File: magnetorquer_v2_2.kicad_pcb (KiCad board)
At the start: 2 copper layers, 89.9 x 96 mm, 25 parts, among them J1 Conn_01x07_Female, U1 MSP430FR5994IPN, U2 Payload, U3 LSM6DS3TR-C, U4 DRV_H3, U5 DRV_H2, U6 DRV_H1, Y1 Crystal

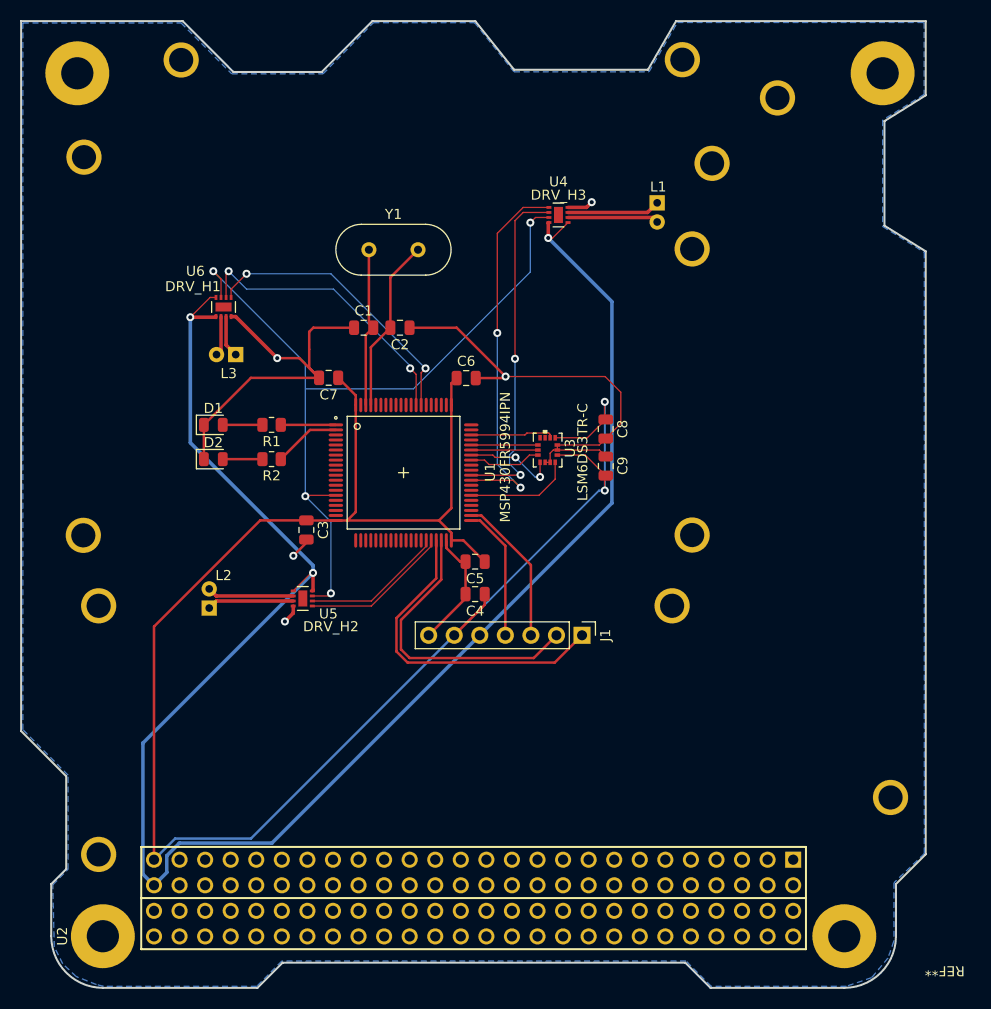
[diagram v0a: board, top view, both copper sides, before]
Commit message: added coils
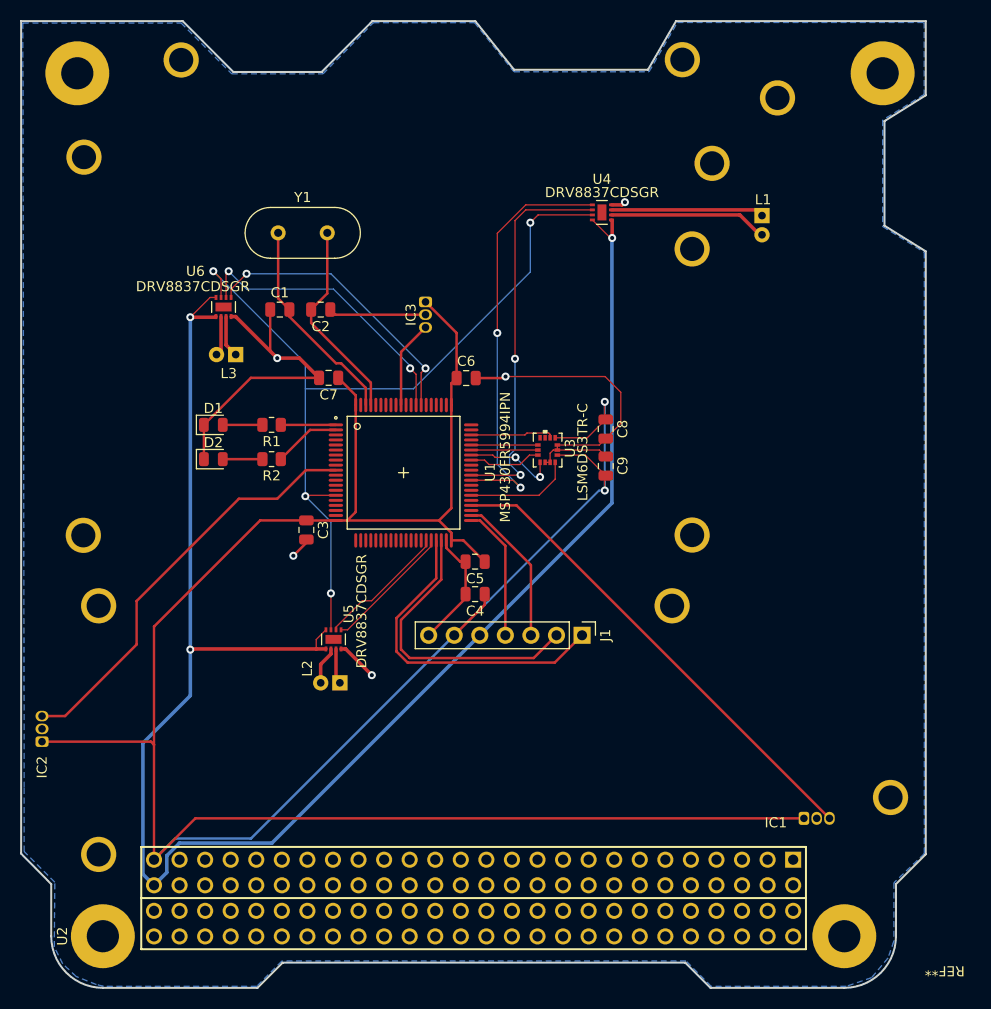
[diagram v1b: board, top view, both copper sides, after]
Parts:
- added IC1: AH9247Z3-G1, Package_TO_SOT_THT:TO-92Flat, B.Cu at (169.7, 135.9)
- added IC2: AH9247Z3-G1, Package_TO_SOT_THT:TO-92Flat, B.Cu at (94.0, 128.3)
- added IC3: AH9247Z3-G1, Package_TO_SOT_THT:TO-92Flat, B.Cu at (132.1, 84.6)
- U4: value DRV_H3 -> DRV8837CDSGR
- U5: value DRV_H2 -> DRV8837CDSGR
- U6: value DRV_H1 -> DRV8837CDSGR
- moved L1 10.5 mm to (159.6, 77.0)
- moved Y1 9.17 mm to (117.4, 77.7)
- moved C1 8.52 mm to (117.6, 85.3)
- moved C2 8.08 mm to (121.7, 85.3)
- moved L2 6.61 mm to (122.6, 116.5), turned to 0 degrees
- moved U5 5.08 mm to (122.9, 118.1), turned to 90 degrees
- moved U4 4.33 mm to (149.6, 75.7)
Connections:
- U1 pad 10: unconnected-(U1-Pad10) -> MAG_2
- U1 pad 44: unconnected-(U1-Pad44) -> MAG_1
- U1 pad 71: unconnected-(U1-Pad71) -> MAG_3
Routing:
- net +3V3: track 181.5 -> 267.9 mm
- net MAG_1: track 0.00 -> 48.5 mm
- net MAG_2: track 0.00 -> 41.8 mm
- net MAG_3: track 0.00 -> 8.71 mm
- net Net-(L1-Pad1): track 9.04 -> 15.8 mm
- net nSLEEP: track 78.9 -> 85.0 mm
- net Net-(L1-Pad2): track 9.25 -> 15.2 mm
- net GND: track 101.1 -> 95.9 mm
- net Net-(L2-Pad2): track 8.64 -> 3.53 mm
- net Net-(C1-Pad2): track 15.9 -> 21.0 mm
- net Net-(L2-Pad1): track 8.64 -> 3.79 mm
- net H1_IN2: track 37.6 -> 42.0 mm
- net H1_IN1: track 34.6 -> 39.0 mm
- net Net-(C2-Pad2): track 17.4 -> 20.2 mm
- net H2_IN2: track 14.8 -> 13.0 mm
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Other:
- outline, holes or cut-outs redrawn

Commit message: new uc
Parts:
- added .: LOGO, magnetorquer:logo, B.Cu at (167.4, 92.9)
- added ?: , , F.Cu at (114.1, 119.1)
- added ?: , , F.Cu at (108.7, 86.1)
- added ?: , , F.Cu at (150.5, 78.3)
- added J2: Conn_02x02_Odd_Even, Connector_PinHeader_2.54mm:PinHeader_2x02_P2.54mm_Vertical, F.Cu at (102.6, 129.2)
- added R3: 0, Resistor_SMD:R_0805_2012Metric, F.Cu at (151.9, 131.2)
- added R4: 0, Resistor_SMD:R_0805_2012Metric, F.Cu at (153.9, 131.2)
- added R5: 0, Resistor_SMD:R_0805_2012Metric, F.Cu at (155.9, 131.3)
- added R6: 0, Resistor_SMD:R_0805_2012Metric, F.Cu at (157.9, 131.3)
- C3: footprint Capacitor_SMD:C_0805_2012Metric -> Capacitor_Tantalum_SMD:CP_EIA-3216-18_Kemet-A
- D1, D2: footprint LED_SMD:LED_0805_2012Metric -> LED_SMD:LED_0603_1608Metric
- U1: value MSP430FR5994IPN -> MSP430FR6972IPM; footprint magnetorquer:MSP430FR5994IPN -> magnetorquer:MSP430FR6972IPM
- moved D2 52.7 mm to (163.3, 93.5), turned to 180 degrees
- moved D1 52.7 mm to (163.3, 90.2), turned to 180 degrees
- moved R1 38.8 mm to (155.1, 90.2), turned to 0 degrees
- moved R2 38.8 mm to (155.0, 93.5), turned to 0 degrees
- moved J1 38.1 mm to (115.6, 97.1), turned to 0 degrees
- moved C3 29.4 mm to (147.9, 97.3), turned to 90 degrees
- moved C4 17.9 mm to (120.9, 105.9), turned to 90 degrees
- moved C5 16.3 mm to (136.9, 94.1), turned to 90 degrees
- moved C8 5.94 mm to (147.9, 102.8)
- moved C9 5.94 mm to (147.9, 106.5)
- moved U3 5.94 mm to (142.2, 104.9)
- moved C6 4.63 mm to (140.3, 94.1), turned to 90 degrees
- moved C7 2.50 mm to (124.7, 91.1), turned to 0 degrees
- moved U1 1.46 mm to (128.9, 100.5)
- moved C1 1.45 mm to (118.1, 84.0), turned to 180 degrees
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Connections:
- J1 pad 5: +5V -> unconnected-(J1-Pad5)
- U1 pad 1: Net-(R1-Pad1) -> BCLUART_RXD
- U1 pad 10: MAG_2 -> unconnected-(U1-Pad10)
- U1 pad 11: unconnected-(U1-Pad11) -> nSLEEP
- U1 pad 14: unconnected-(U1-Pad14) -> H2_IN2
- U1 pad 15: nSLEEP -> H2_IN1
- U1 pad 17: unconnected-(U1-Pad17) -> GND
- U1 pad 18: unconnected-(U1-Pad18) -> +3V3
- U1 pad 19: unconnected-(U1-Pad19) -> SBWTCK
- U1 pad 2: Net-(R2-Pad1) -> unconnected-(U1-Pad2)
- U1 pad 20: +3V3 -> SBWTDIO
- U1 pad 26: unconnected-(U1-Pad26) -> Net-(U1-Pad26)
- U1 pad 27: unconnected-(U1-Pad27) -> Net-(U1-Pad27)
- U1 pad 28: unconnected-(U1-Pad28) -> Net-(U1-Pad28)
- U1 pad 29: unconnected-(U1-Pad29) -> Net-(U1-Pad29)
- U1 pad 30: unconnected-(U1-Pad30) -> ATT_CS
- U1 pad 31: unconnected-(U1-Pad31) -> ATT_SCL
- U1 pad 32: unconnected-(U1-Pad32) -> ATT_SDO
- U1 pad 33: unconnected-(U1-Pad33) -> ATT_SDI
- U1 pad 34: unconnected-(U1-Pad34) -> ATT_INT2
- U1 pad 35: H2_IN1 -> ATT_INT1
- U1 pad 36: H2_IN2 -> H1_IN1
- U1 pad 37: SBWTCK -> H1_IN2
- U1 pad 38: SBWTDIO -> unconnected-(U1-Pad38)
- U1 pad 41: BCLUART_TXD -> unconnected-(U1-Pad41)
- U1 pad 42: BCLUART_RXD -> unconnected-(U1-Pad42)
- U1 pad 43: unconnected-(U1-Pad43) -> Net-(R2-Pad1)
- U1 pad 44: MAG_1 -> Net-(R1-Pad1)
- U1 pad 45: unconnected-(U1-Pad45) -> MAG_3
- U1 pad 46: ATT_INT1 -> MAG_2
- U1 pad 47: unconnected-(U1-Pad47) -> MAG_1
- U1 pad 49: H1_IN2 -> +3V3
- U1 pad 50: H1_IN1 -> GND
- U1 pad 51: unconnected-(U1-Pad51) -> Net-(C2-Pad2)
- U1 pad 52: unconnected-(U1-Pad52) -> Net-(C1-Pad2)
- U1 pad 53: ATT_SDI -> GND
- U1 pad 54: ATT_SDO -> unconnected-(U1-Pad54)
- U1 pad 55: ATT_SCL -> unconnected-(U1-Pad55)
- U1 pad 56: ATT_CS -> GND
- U1 pad 58: ATT_INT2 -> unconnected-(U1-Pad58)
- U1 pad 60: unconnected-(U1-Pad60) -> H3_IN1
- U1 pad 61: +3V3 -> H3_IN2
- U1 pad 62: unconnected-(U1-Pad62) -> GND
- U1 pad 63: unconnected-(U1-Pad63) -> +3V3
- U1 pad 64: unconnected-(U1-Pad64) -> BCLUART_TXD
- U2 pad 10: unconnected-(U2-Pad10) -> SPI-MISO
- U2 pad 11: unconnected-(U2-Pad11) -> SPI-MOSI
- U2 pad 12: unconnected-(U2-Pad12) -> SPI-CS
- U2 pad 51: +3V3 -> +5V
- U2 pad 52: +5V -> +3V3
- U2 pad 9: unconnected-(U2-Pad9) -> SPI-CLK
- U4 pad 1: +5V -> DRV_VM
- U4 pad 8: +5V -> DRV_VM
- U5 pad 1: +5V -> DRV_VM
- U5 pad 8: +5V -> DRV_VM
- U6 pad 1: +5V -> DRV_VM
- U6 pad 8: +5V -> DRV_VM
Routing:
- net +5V: track 173.7 -> 8.31 mm, vias 3 -> 0
- net DRV_VM: track 0.00 -> 139.5 mm
- net MAG_2: track 41.8 -> 136.6 mm, vias 0 -> 1
- net Net-(U1-Pad29): track 0.00 -> 39.4 mm
- net Net-(U1-Pad28): track 0.00 -> 38.6 mm
- net Net-(U1-Pad27): track 0.00 -> 37.2 mm
- net Net-(U1-Pad26): track 0.00 -> 36.0 mm
- net GND: track 95.9 -> 122.9 mm, vias 5 -> 8
- net nSLEEP: track 85.0 -> 105.1 mm
- net Net-(R1-Pad1): track 5.47 -> 23.2 mm
- net SPI-CS: track 0.00 -> 16.2 mm, vias 0 -> 2
- net Net-(R2-Pad1): track 6.67 -> 22.0 mm
- net MAG_3: track 8.71 -> 23.8 mm, vias 0 -> 2
- net +3V3: track 267.9 -> 282.7 mm, vias 2 -> 1
- net SPI-MISO: track 0.00 -> 12.3 mm
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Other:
- board text added: "+3V3"
- board text added: "3V3"
- board text added: "5V"
- board text added: "Aluno: Li Wing Kee Ramos Professor: Daniel Chaves Café"
- board text added: "GND"
- board text added: "NC"
- board text added: "RX"
- board text added: "SBWDIO"
- board text added: "SBWTCK"
- board text added: "TX"
